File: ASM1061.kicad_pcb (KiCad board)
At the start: 4 copper layers, 54 x 48.1 mm, 51 parts, among them J1 Bus_PCI_Express_x1, J2 Conn_01x07_MountingPin, J3 Conn_01x07_MountingPin, U1 IS25LQ512B, U2 ASM1061, Y1 Crystal_GND24

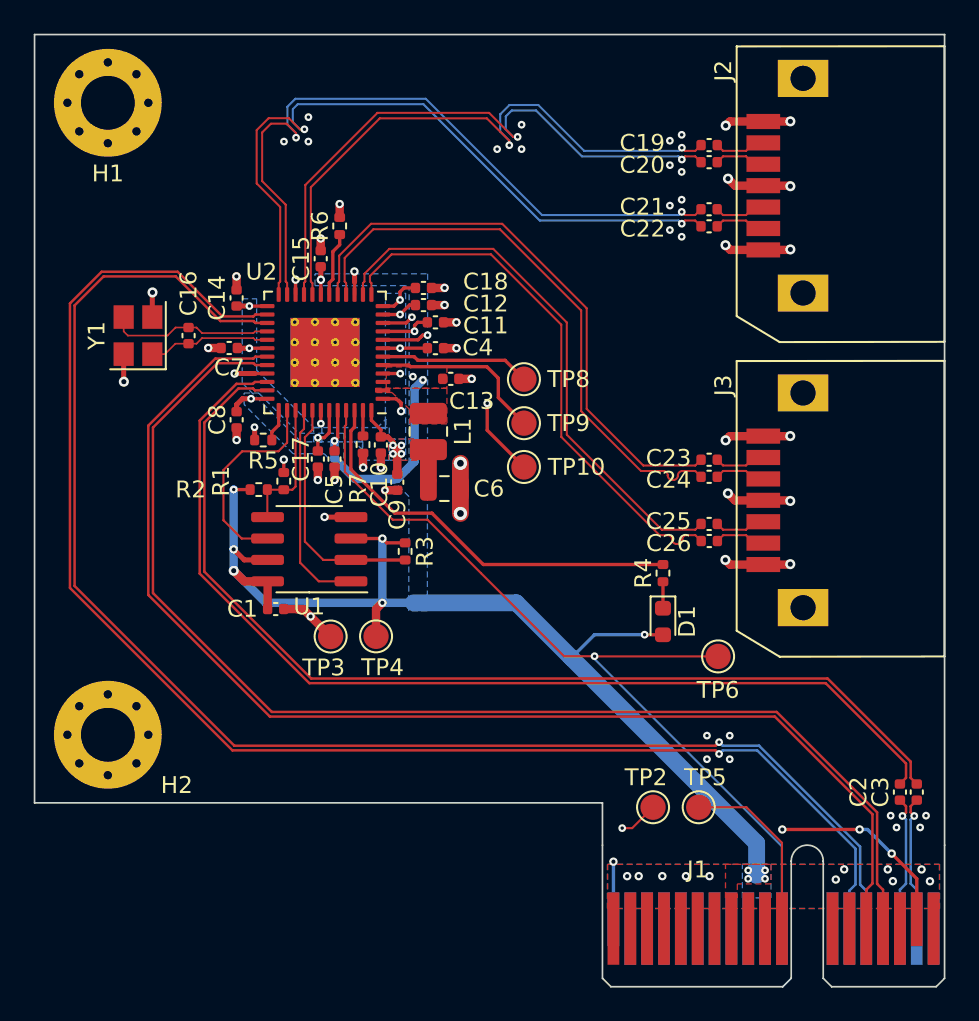
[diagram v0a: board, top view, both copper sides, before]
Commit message: use solid ground pour for asm1061, increase power trace size
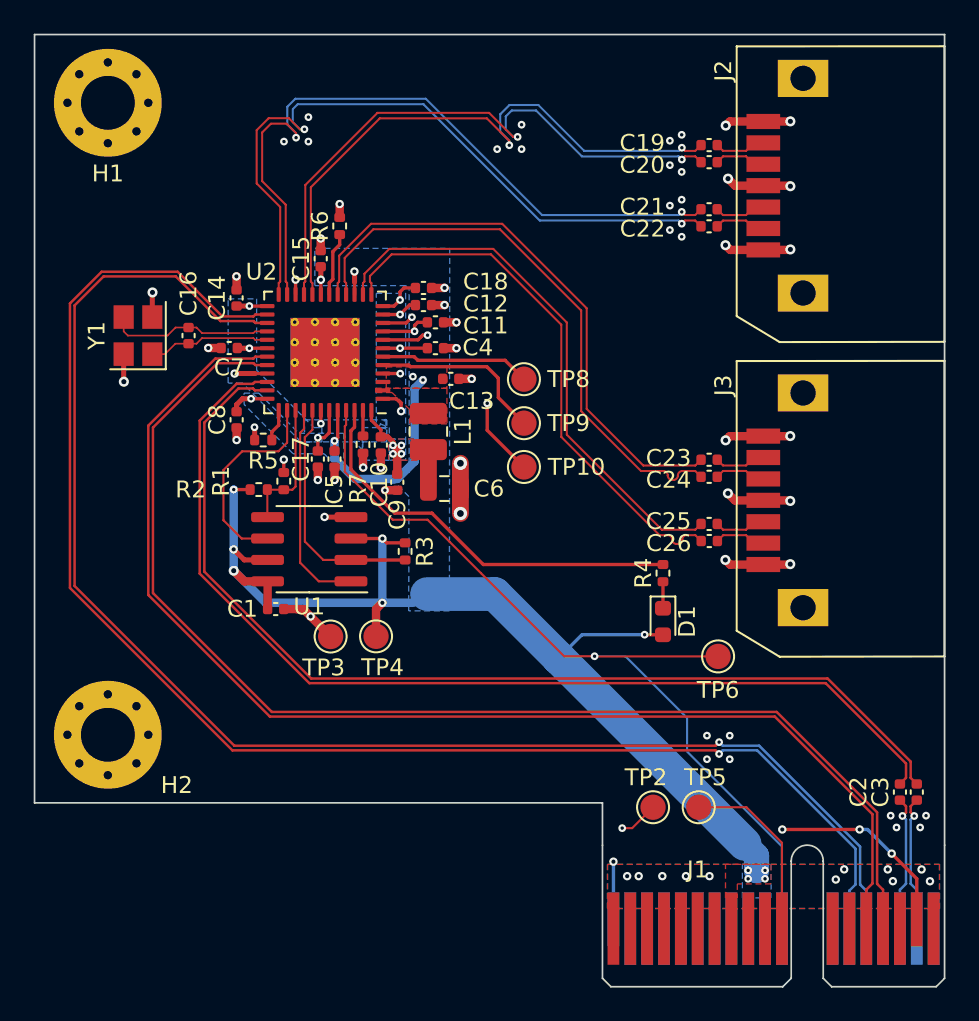
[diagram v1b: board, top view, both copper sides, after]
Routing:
- net /PCIe_nRST: track 51.1 -> 52.2 mm
- net /+3.3V: track 88.3 -> 87.7 mm
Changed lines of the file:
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@@
     (property "Sheetfile" "ASM1061.kicad_sch")
     (property "Sheetname" "")
+    (zone_connect 2)
     (attr smd)
     (fp_text reference "U2" (at 3.778049 4.783761 180) (layer "F.SilkS")
@@
   (via (at 115.35 104.06) (size 0.46) (drill 0.2) (layers "F.Cu" "B.Cu") (net 2))
   (via (at 99.79 102.17) (size 0.5) (drill 0.24) (layers "F.Cu" "B.Cu") (net 2))
+  (segment (start 106.46 101.65) (end 102.44 101.65) (width 2) (layer "B.Cu") (net 2))
   (segment (start 90.967929 98.997383) (end 90.967929 95.452071) (width 0.5) (layer "B.Cu") (net 2))
   (segment (start 99.79 102.17) (end 99.79 98.36) (width 0.5) (layer "B.Cu") (net 2))
   (segment (start 96.95 93.6) (end 96.95 92.56) (width 0.5) (layer "B.Cu") (net 2))
+  (segment (start 111.64 104.06) (end 110.255 105.445) (width 0.2) (layer "B.Cu") (net 2))
   (segment (start 100.67 94.82) (end 98.17 94.82) (width 0.5) (layer "B.Cu") (net 2))
   (segment (start 101.7 93.79) (end 100.67 94.82) (width 0.5) (layer "B.Cu") (net 2))
-  (segment (start 111.005 105.435) (end 121.998954 116.428954) (width 1) (layer "B.Cu") (net 2))
   (segment (start 90.967575 100.264364) (end 90.967575 98.997737) (width 0.5) (layer "B.Cu") (net 2))
   (segment (start 101.7 93.79) (end 101.7 89.445613) (width 0.5) (layer "B.Cu") (net 2))
-  (segment (start 101.63 102.17) (end 107.74 102.17) (width 1) (layer "B.Cu") (net 2))
-  (segment (start 112.38 104.06) (end 111.005 105.435) (width 0.2) (layer "B.Cu") (net 2))
+  (segment (start 121.29 116.48) (end 110.255 105.445) (width 2) (layer "B.Cu") (net 2))
+  (segment (start 121.99 117.18) (end 121.99 118.07) (width 1.5) (layer "B.Cu") (net 2))
   (segment (start 92.873211 102.17) (end 90.967575 100.264364) (width 0.5) (layer "B.Cu") (net 2))
+  (segment (start 121.29 116.48) (end 121.99 117.18) (width 1.5) (layer "B.Cu") (net 2))
   (segment (start 90.967575 98.997737) (end 90.967929 98.997383) (width 0.5) (layer "B.Cu") (net 2))
-  (segment (start 107.74 102.17) (end 111.005 105.435) (width 1) (layer "B.Cu") (net 2))
   (segment (start 99.79 102.17) (end 101.63 102.17) (width 0.5) (layer "B.Cu") (net 2))
   (segment (start 101.7 89.445613) (end 102.19823 88.947383) (width 0.5) (layer "B.Cu") (net 2))
-  (segment (start 121.998954 116.428954) (end 121.998954 118.351863) (width 1) (layer "B.Cu") (net 2))
-  (segment (start 115.35 104.06) (end 112.38 104.06) (width 0.2) (layer "B.Cu") (net 2))
+  (segment (start 110.255 105.445) (end 106.46 101.65) (width 2) (layer "B.Cu") (net 2))
   (segment (start 90.967929 95.452071) (end 90.97 95.45) (width 0.5) (layer "B.Cu") (net 2))
+  (segment (start 115.35 104.06) (end 111.64 104.06) (width 0.2) (layer "B.Cu") (net 2))
   (segment (start 99.79 102.17) (end 92.873211 102.17) (width 0.5) (layer "B.Cu") (net 2))
   (segment (start 98.17 94.82) (end 96.95 93.6) (width 0.5) (layer "B.Cu") (net 2))
@@
   (segment (start 100.4 97.24) (end 100.96 97.24) (width 0.127) (layer "F.Cu") (net 20))
   (via (at 112.38 105.34) (size 0.46) (drill 0.2) (layers "F.Cu" "B.Cu") (net 20))
-  (segment (start 112.38 105.5) (end 123.5 116.62) (width 0.127) (layer "B.Cu") (net 20))
-  (segment (start 112.38 105.34) (end 112.38 105.5) (width 0.127) (layer "B.Cu") (net 20))
   (segment (start 123.5 116.62) (end 123.5 121.5) (width 0.127) (layer "B.Cu") (net 20))
+  (segment (start 117.87 109) (end 117.87 110.99) (width 0.127) (layer "B.Cu") (net 20))
+  (segment (start 117.87 110.99) (end 123.5 116.62) (width 0.127) (layer "B.Cu") (net 20))
+  (segment (start 112.38 105.34) (end 114.21 105.34) (width 0.127) (layer "B.Cu") (net 20))
+  (segment (start 114.21 105.34) (end 117.87 109) (width 0.127) (layer "B.Cu") (net 20))
   (segment (start 87.645232 82.525712) (end 83.130866 82.525712) (width 0.149098) (layer "F.Cu") (net 21))
   (segment (start 92.138049 85.175712) (end 90.295232 85.175712) (width 0.149098) (layer "F.Cu") (net 21))
@@
         (xy 99.97 92.46)
         (xy 99.97 91.67)
-        (xy 99.97 91.47)
-        (xy 99.97 83.805791)
+        (xy 99.43 91.47)
+        (xy 99.43 83.805791)
         (xy 101.17 83.805791)
       )
@@
         (xy 96.2 92.62)
         (xy 94.967597 92.62)
-        (xy 91.472129 89.124532)
-        (xy 91.472129 84.13)
+        (xy 93.219863 90.872266)
+        (xy 92.345996 89.998399)
+        (xy 91.47 89.124532)
+        (xy 90.64 89.13)
+        (xy 90.642113 84.13)
         (xy 92.33 84.13)
       )
@@
     (polygon
       (pts
-        (xy 102.456824 102.648452)
+        (xy 103.766823 102.649773)
         (xy 101.349984 102.645786)
         (xy 101.369342 95.87)
@@
         (xy 101.17 83.35)
         (xy 95.79 83.35)
-        (xy 95.79 82.646969)
-        (xy 102.476987 82.64715)
+        (xy 95.790282 81.137316)
+        (xy 103.787268 81.138818)
       )
     )
@@
     (polygon
       (pts
-        (xy 98.6 92.62)
-        (xy 95.71 92.62)
-        (xy 95.71 91.77)
-        (xy 98.6 91.77)
+        (xy 100.05 92.62)
+        (xy 95.17 92.62)
+        (xy 95.17 91.31)
+        (xy 100.05 91.31)
       )
     )
@@
   )
   (zone (net 11) (net_name "/ASM_1.2V") (layer "B.Cu") (hatch edge 0.508)
-    (connect_pads yes (clearance 0.254))
+    (connect_pads yes (clearance 0.2))
     (min_thickness 0.254) (filled_areas_thickness no)
     (fill yes (thermal_gap 0.508) (thermal_bridge_width 0.508))
